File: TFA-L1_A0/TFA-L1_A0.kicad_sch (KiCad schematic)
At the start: 5 parts, among them U1 AMS1117-3.3

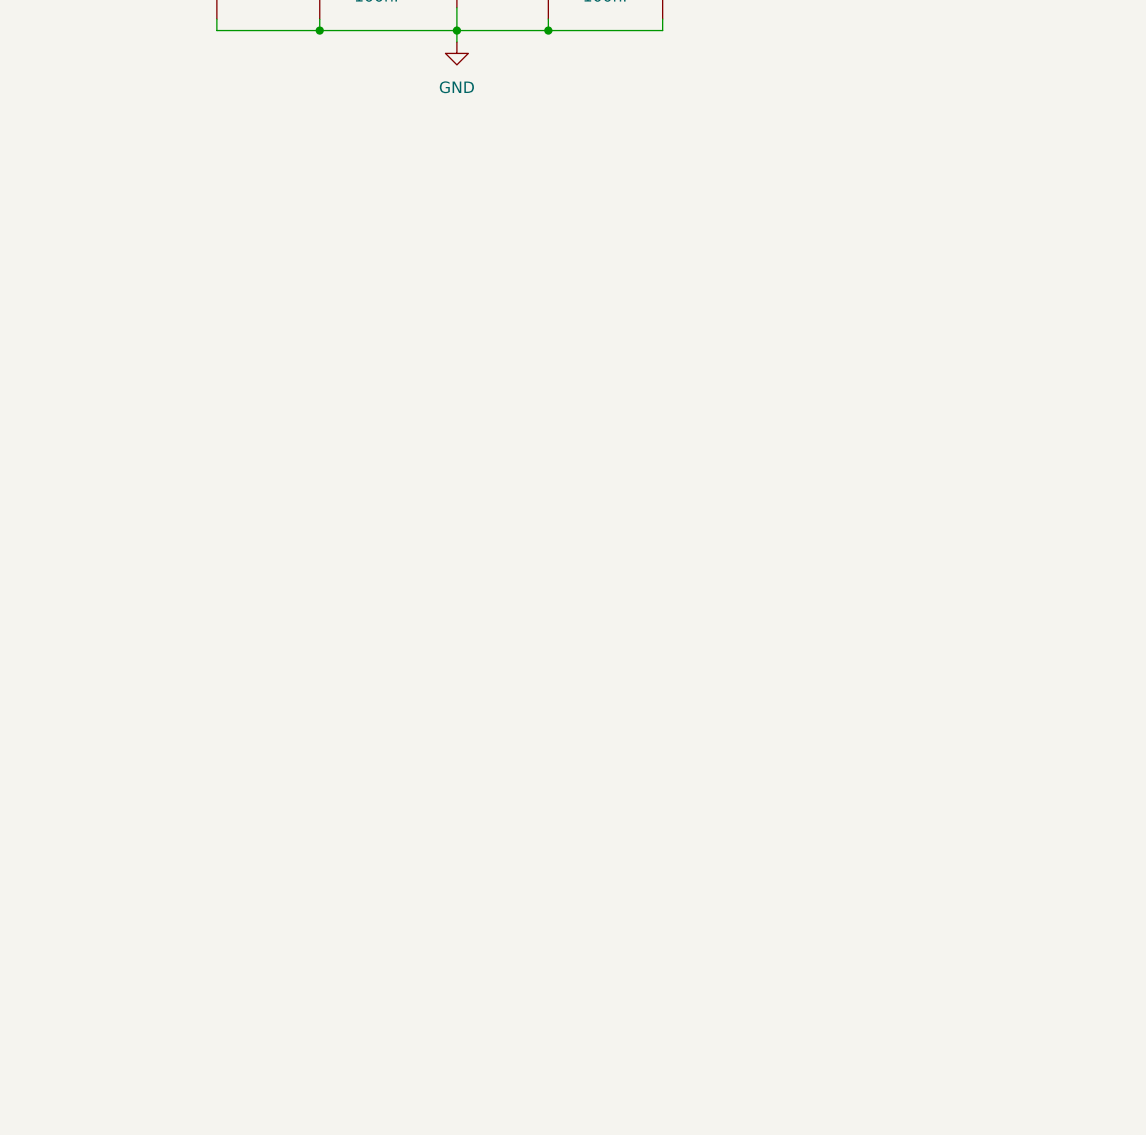
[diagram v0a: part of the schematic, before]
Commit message: feat: Add output component
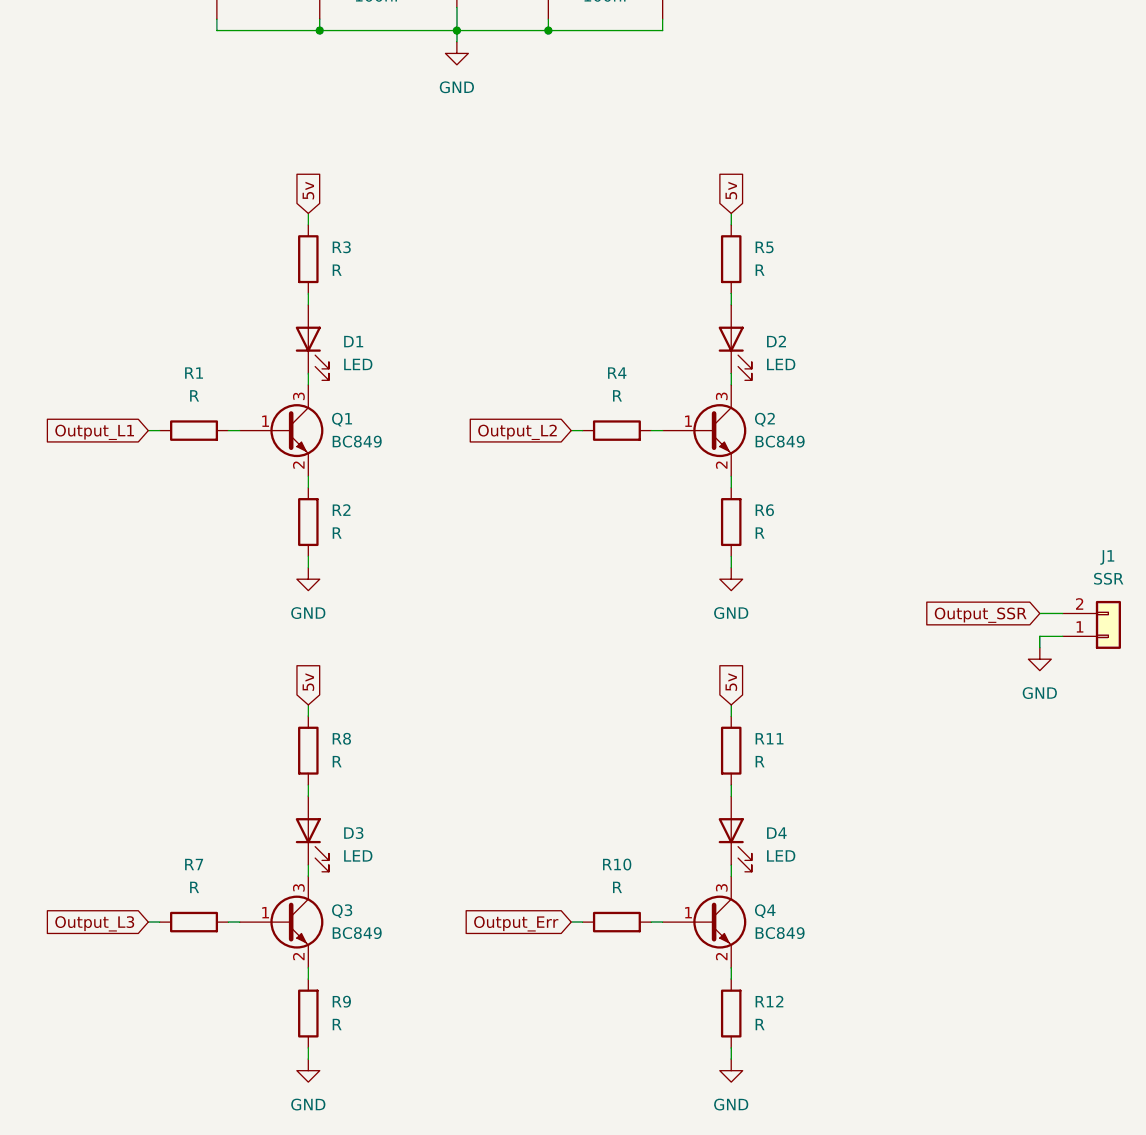
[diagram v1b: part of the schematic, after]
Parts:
- added D1, D2, D3, D4: LED, symbol Device:LED
- added J1: SSR, TerminalBlock:TerminalBlock_bornier-2_P5.08mm, symbol Connector_Generic:Conn_01x02
- added Q1, Q2, Q3, Q4: BC849, Package_TO_SOT_SMD:SOT-23, symbol Transistor_BJT:BC849
- added R1, R10, R11, R12, R2, R3, R4, R5, R6, R7, R8, R9: R, symbol Device:R
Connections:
- net 5v: now also R11.1, R3.1, R5.1, R8.1
- net GND: now also J1.1 (Pin_1), R12.1, R2.1, R6.1, R9.1
- new net: Q4.1 (B), R10.2
- new net: Q3.1 (B), R7.2
- new net: D4.2 (A), R11.2
- new net: D4.1 (K), Q4.3 (C)
- new net: Q2.1 (B), R4.2
- new net: Q3.2 (E), R9.2
- new net: D3.1 (K), Q3.3 (C)
- new net: D1.2 (A), R3.2
- new net: D2.1 (K), Q2.3 (C)
- new net: D2.2 (A), R5.2
- new net: Q1.2 (E), R2.2
- new net: D1.1 (K), Q1.3 (C)
- new net: D3.2 (A), R8.2
- new net: Q2.2 (E), R6.2
- new net: Q1.1 (B), R1.2
- new net: Q4.2 (E), R12.2
- new net Output_Err: R10.1
- new net Output_L1: R1.1
- new net Output_L2: R4.1
- new net Output_L3: R7.1
- new net Output_SSR: J1.2 (Pin_2)

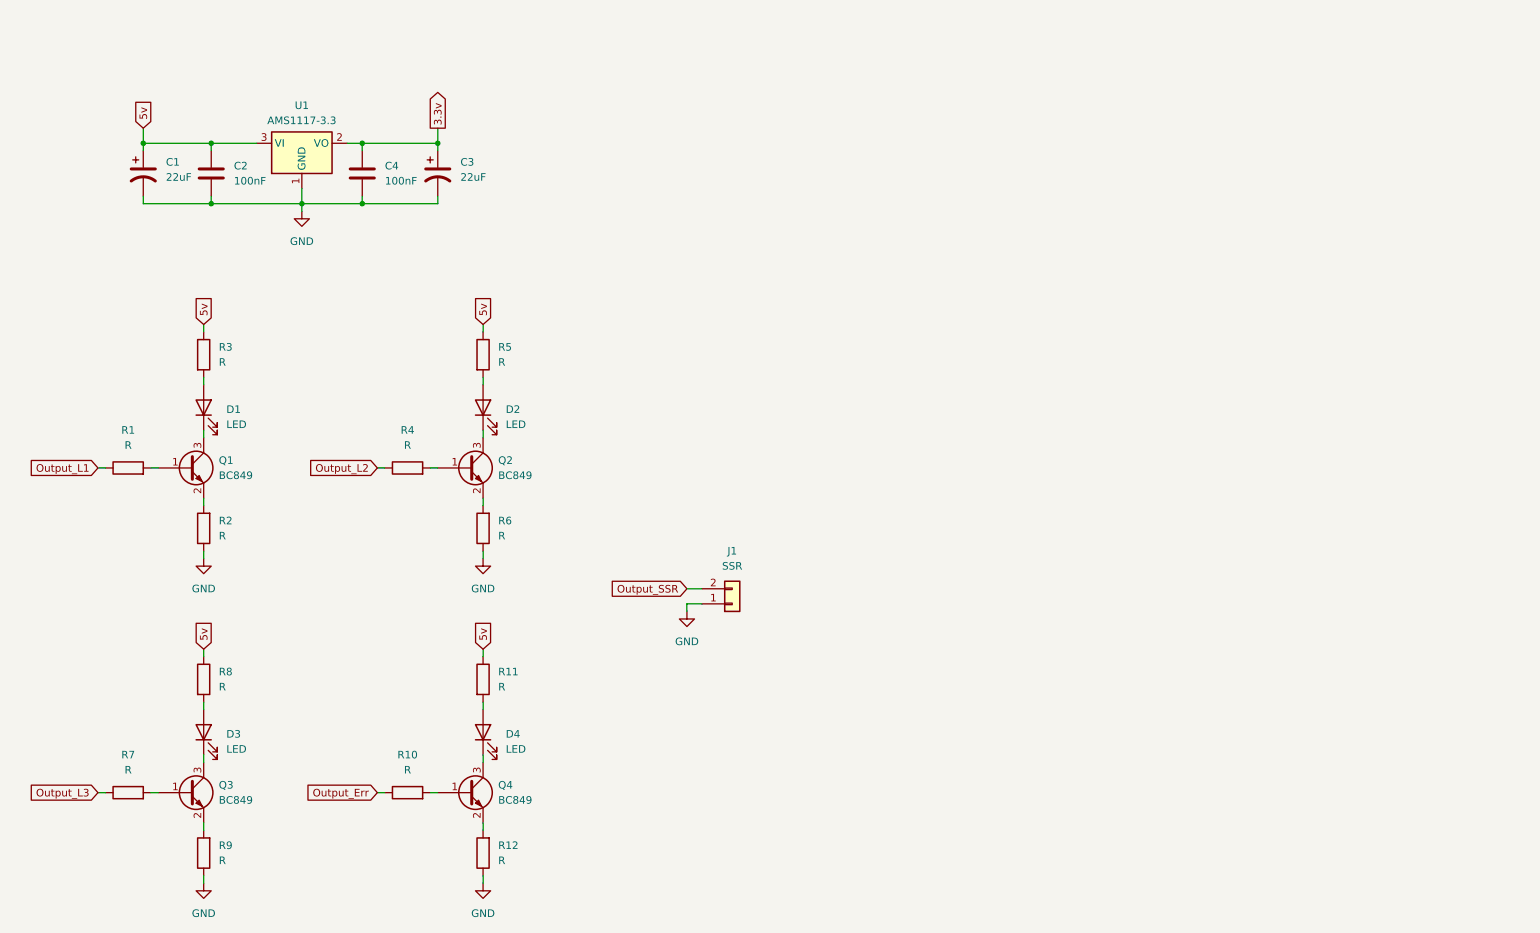
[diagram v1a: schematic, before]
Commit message: feat: Add microcontroller
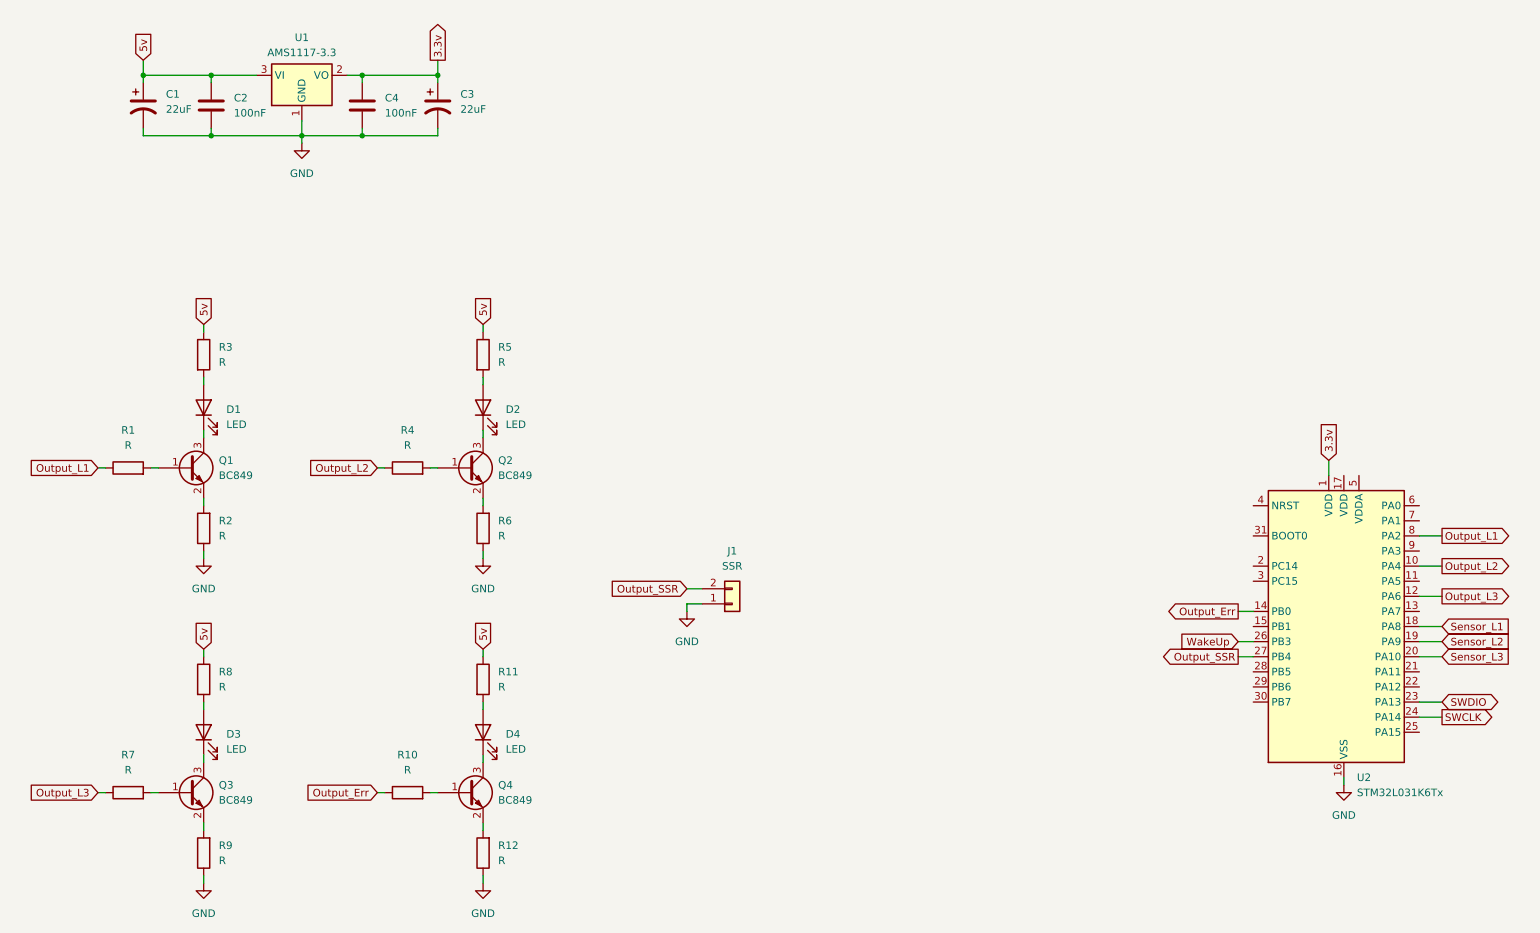
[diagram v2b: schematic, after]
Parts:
- added U2: STM32L031K6Tx, Package_QFP:LQFP-32_7x7mm_P0.8mm, symbol MCU_ST_STM32L0:STM32L031K6Tx
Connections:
- net 3.3v: now also U2.1 (VDD)
- net GND: now also U2.16 (VSS), U2.32 (VSS)
- net Output_Err: now also U2.14 (PB0)
- net Output_L1: now also U2.8 (PA2)
- net Output_L2: now also U2.10 (PA4)
- net Output_L3: now also U2.12 (PA6)
- net Output_SSR: now also U2.27 (PB4)
- new net SWCLK: U2.24 (PA14)
- new net SWDIO: U2.23 (PA13)
- new net Sensor_L1: U2.18 (PA8)
- new net Sensor_L2: U2.19 (PA9)
- new net Sensor_L3: U2.20 (PA10)
- new net WakeUp: U2.26 (PB3)
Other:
- moved on the sheet: C1, C2, C3, C4, U1
